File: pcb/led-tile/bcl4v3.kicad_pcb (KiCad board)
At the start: 2 copper layers, 38 x 38 mm, 36 parts, among them J1 Conn_01x04, J10 Conn_01x04, J2 Conn_01x04, J3 Conn_01x04, J4 Conn_01x04, J5 Conn_01x04, J6 Conn_01x04, J7 Conn_01x04, J8 Conn_01x04, J9 10118194-0001LF, Q1 IRLML6402, U1 STM32F072CBTx, U2 74HC595D_118, U3 TBD62783A, U4 TLC5916ID, U5 MCP1703A-3302_SOT23, Y1 ABS07-120-32.768KHZ-Z

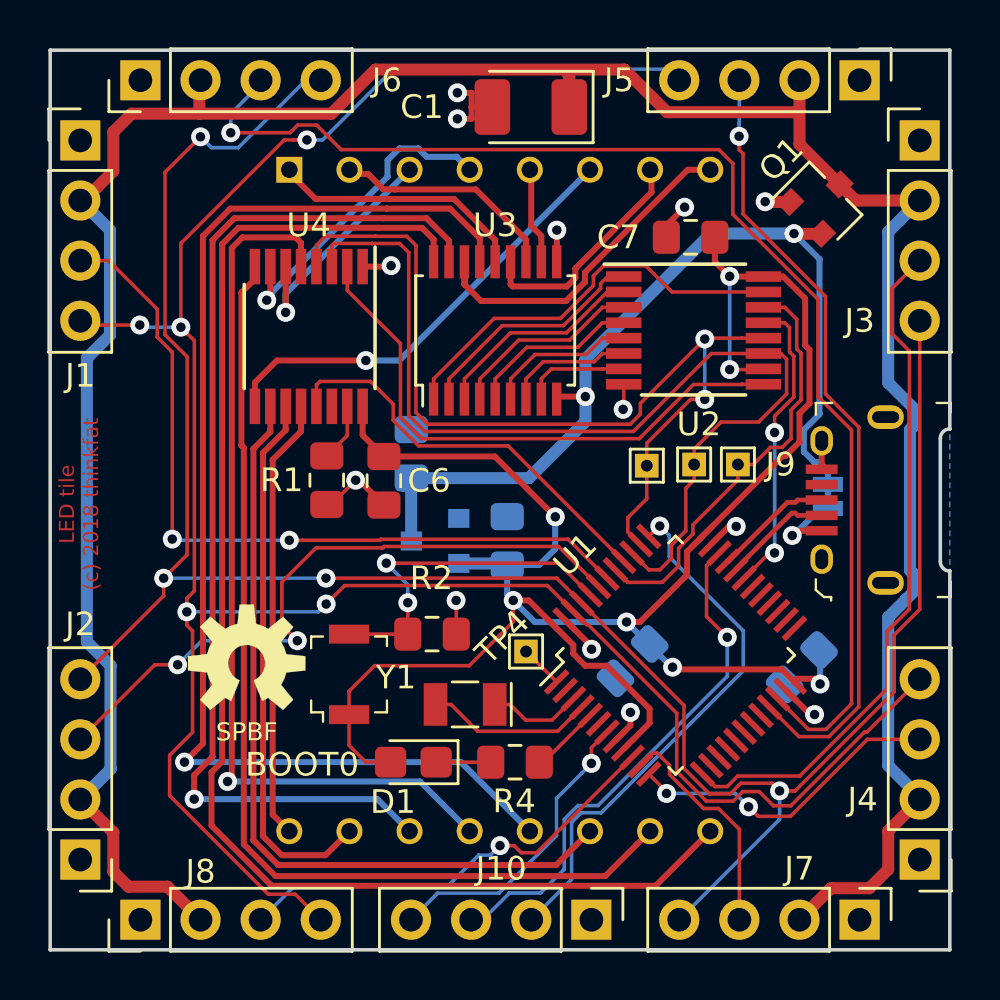
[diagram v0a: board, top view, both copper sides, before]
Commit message: pcb: put USB_VBUS to pin header
Replace one pin header with a 5-contact version and route USB_VBUS
to this pin. Necessary to power a plug-on battery shield from the main
USB connector.
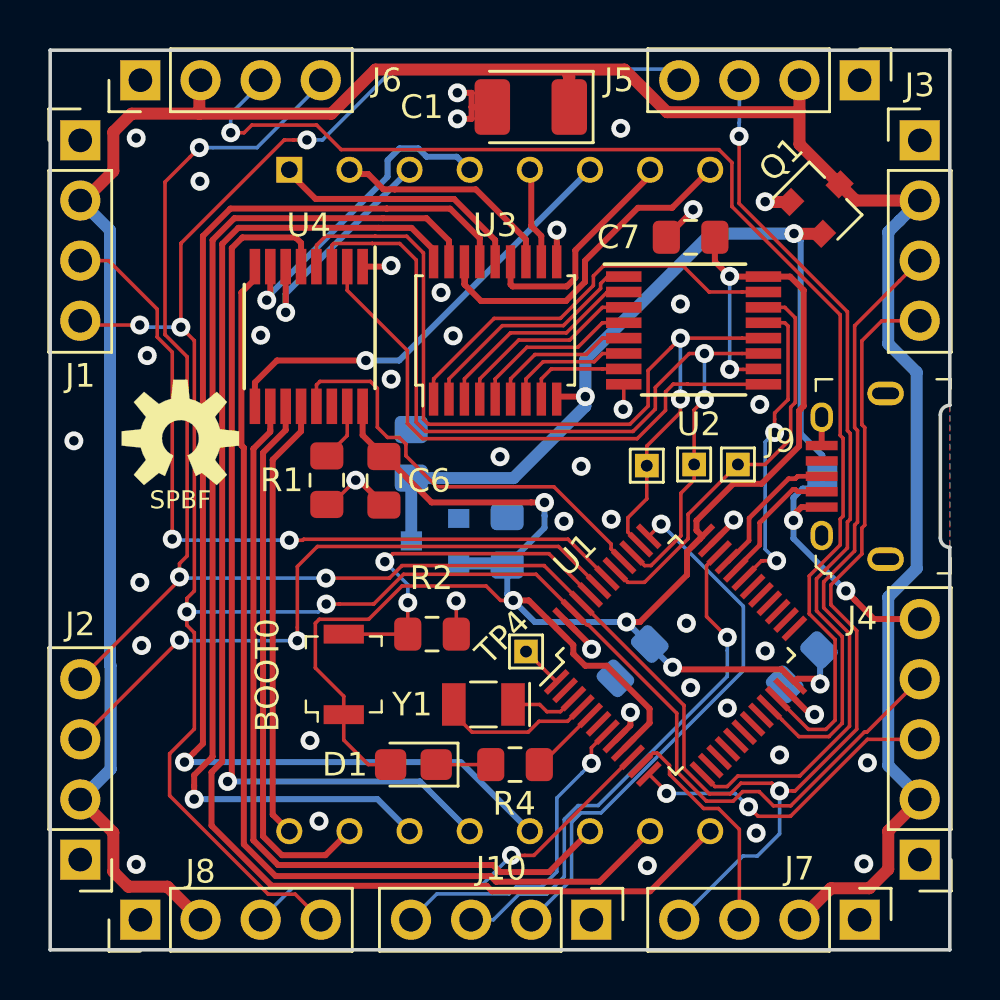
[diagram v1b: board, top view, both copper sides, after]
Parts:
- J4: value Conn_01x04 -> Conn_01x05; footprint Connector_PinHeader_2.54mm:PinHeader_1x04_P2.54mm_Vertical -> Connector_PinHeader_2.54mm:PinHeader_1x05_P2.54mm_Vertical
- moved LOGO1 9.90 mm to (119.5, 80.4)
- moved J9 1.00 mm to (146.6, 82.0)
- moved JP1 0.87 mm to (146.6, 82.0)
- moved Y1 0.77 mm to (132.3, 91.6)
- moved BOOT0 0.22 mm to (126.4, 90.4)
- moved D1 0.10 mm to (129.3, 94.2)
- moved R4 0.10 mm to (133.6, 94.2)
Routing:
- net /USB_VBUS: track 3.51 -> 11.7 mm, vias 1 -> 2
- net +3V3: track 86.0 -> 89.4 mm
- net /CAT_CLK: track 42.4 -> 39.3 mm, vias 0 -> 2
- net +5V: track 39.0 -> 37.0 mm
- net /SYN_RX: track 94.0 -> 95.5 mm
- net /OSC_IN: track 3.97 -> 2.91 mm
- net /nOE_COL: track 17.5 -> 18.5 mm
- net /USB_D+: track 5.05 -> 6.02 mm
- net /USB_D-: track 4.68 -> 5.65 mm
- net /nRST: track 12.9 -> 13.8 mm
- net VCC: track 117.1 -> 116.3 mm
- net /CAT_DATA: track 18.1 -> 17.5 mm
- net /UART3_RX: track 53.6 -> 54.2 mm
- net /UART3_TX: track 33.4 -> 34.0 mm
- net /UART1_RX: track 28.3 -> 27.8 mm
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- added copper zone on F.Cu, net GND
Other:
- outline, holes or cut-outs redrawn
- board text added: "LED tile ©2019 thinkfat"
- board text removed: "LED tile (c) 2018 thinkfat"

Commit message: pcb: update led-tile to latest version
move OSHW logo into a project specific library as not everyone has the
Sparkfun Libraries installed, decrease current through the SMD LED,
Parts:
- LOGO1: footprint Aesthetics:OSHW-LOGO-M -> project:OSHW-LOGO-M
- R4: value 680R -> 715R
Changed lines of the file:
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@@
     (add_net /ROW_8)
+  )
+  (module project:OSHW-LOGO-M (layer F.Cu)
+    (at 119.5 80.4)
+    (descr "OPEN-SOURCE HARDWARE (OSHW) LOGO - MEDIUM - SILKSCREEN")
+    (tags "OPEN-SOURCE HARDWARE (OSHW) LOGO - MEDIUM - SILKSCREEN")
+    (attr virtual)
+    (fp_text reference LOGO1 (at 0 0) (layer F.SilkS) hide
+      (effects (font (size 1 1) (thickness 0.15)))
+    )
+    (fp_text value OSHW-LOGOM (at 0 0) (layer F.SilkS) hide
+      (effects (font (size 1.524 1.524) (thickness 0.15)))
+    )
+    (fp_poly (pts (xy 0.65532 1.5875) (xy 0.90932 1.45542) (xy 1.5367 1.9685) (xy 1.9685 1.5367)
+      (xy 1.45542 0.90932) (xy 1.5875 0.65532) (xy 1.67386 0.38608) (xy 2.47904 0.30226)
+      (xy 2.47904 -0.30226) (xy 1.67386 -0.38608) (xy 1.5875 -0.65532) (xy 1.45542 -0.90932)
+      (xy 1.9685 -1.5367) (xy 1.5367 -1.9685) (xy 0.90932 -1.45542) (xy 0.65532 -1.5875)
+      (xy 0.38608 -1.67386) (xy 0.30226 -2.47904) (xy -0.30226 -2.47904) (xy -0.38608 -1.67386)
+      (xy -0.65532 -1.5875) (xy -0.90932 -1.45542) (xy -1.5367 -1.9685) (xy -1.9685 -1.5367)
+      (xy -1.45542 -0.90932) (xy -1.5875 -0.65532) (xy -1.67386 -0.38608) (xy -2.47904 -0.30226)
+      (xy -2.47904 0.30226) (xy -1.67386 0.38608) (xy -1.5875 0.65532) (xy -1.45542 0.90932)
+      (xy -1.9685 1.5367) (xy -1.5367 1.9685) (xy -0.90932 1.45542) (xy -0.65532 1.5875)
+      (xy -0.29718 0.72136) (xy -0.4318 0.6477) (xy -0.55118 0.55118) (xy -0.6477 0.4318)
+      (xy -0.72136 0.29718) (xy -0.76454 0.1524) (xy -0.77978 0) (xy -0.76454 -0.15748)
+      (xy -0.71374 -0.31242) (xy -0.635 -0.44958) (xy -0.53086 -0.5715) (xy -0.40132 -0.66802)
+      (xy -0.25654 -0.7366) (xy -0.1016 -0.77216) (xy 0.05588 -0.77724) (xy 0.2159 -0.7493)
+      (xy 0.36322 -0.68834) (xy 0.49784 -0.59944) (xy 0.6096 -0.48514) (xy 0.69596 -0.35052)
+      (xy 0.75438 -0.20066) (xy 0.77978 -0.04318) (xy 0.77216 0.1143) (xy 0.73152 0.26924)
+      (xy 0.6604 0.41402) (xy 0.56134 0.54102) (xy 0.43942 0.64516) (xy 0.29718 0.72136)) (layer F.SilkS) (width 0.01))
   )
   (module Connector_PinHeader_2.54mm:PinHeader_1x04_P2.54mm_Vertical (layer F.Cu)
@@
       (effects (font (size 1 1) (thickness 0.15)))
     )
-    (fp_text value 680R (at 0 1.65) (layer F.Fab)
+    (fp_text value 715R (at 0 1.65) (layer F.Fab)
       (effects (font (size 1 1) (thickness 0.15)))
     )
@@
     (pad 1 thru_hole rect (at 0 0) (size 1 1) (drill 0.5) (layers *.Cu *.Mask)
       (net 12 /CAT_STROBE))
-  )
-  (module Aesthetics:OSHW-LOGO-M (layer F.Cu)
-    (at 119.5 80.4)
-    (descr "OPEN-SOURCE HARDWARE (OSHW) LOGO - MEDIUM - SILKSCREEN")
-    (tags "OPEN-SOURCE HARDWARE (OSHW) LOGO - MEDIUM - SILKSCREEN")
-    (attr virtual)
-    (fp_text reference LOGO1 (at 0 0) (layer F.SilkS) hide
-      (effects (font (size 1 1) (thickness 0.15)))
-    )
-    (fp_text value OSHW-LOGOM (at 0 0) (layer F.SilkS) hide
-      (effects (font (size 1.524 1.524) (thickness 0.15)))
-    )
-    (fp_poly (pts (xy 0.65532 1.5875) (xy 0.90932 1.45542) (xy 1.5367 1.9685) (xy 1.9685 1.5367)
-      (xy 1.45542 0.90932) (xy 1.5875 0.65532) (xy 1.67386 0.38608) (xy 2.47904 0.30226)
-      (xy 2.47904 -0.30226) (xy 1.67386 -0.38608) (xy 1.5875 -0.65532) (xy 1.45542 -0.90932)
-      (xy 1.9685 -1.5367) (xy 1.5367 -1.9685) (xy 0.90932 -1.45542) (xy 0.65532 -1.5875)
-      (xy 0.38608 -1.67386) (xy 0.30226 -2.47904) (xy -0.30226 -2.47904) (xy -0.38608 -1.67386)
-      (xy -0.65532 -1.5875) (xy -0.90932 -1.45542) (xy -1.5367 -1.9685) (xy -1.9685 -1.5367)
-      (xy -1.45542 -0.90932) (xy -1.5875 -0.65532) (xy -1.67386 -0.38608) (xy -2.47904 -0.30226)
-      (xy -2.47904 0.30226) (xy -1.67386 0.38608) (xy -1.5875 0.65532) (xy -1.45542 0.90932)
-      (xy -1.9685 1.5367) (xy -1.5367 1.9685) (xy -0.90932 1.45542) (xy -0.65532 1.5875)
-      (xy -0.29718 0.72136) (xy -0.4318 0.6477) (xy -0.55118 0.55118) (xy -0.6477 0.4318)
-      (xy -0.72136 0.29718) (xy -0.76454 0.1524) (xy -0.77978 0) (xy -0.76454 -0.15748)
-      (xy -0.71374 -0.31242) (xy -0.635 -0.44958) (xy -0.53086 -0.5715) (xy -0.40132 -0.66802)
-      (xy -0.25654 -0.7366) (xy -0.1016 -0.77216) (xy 0.05588 -0.77724) (xy 0.2159 -0.7493)
-      (xy 0.36322 -0.68834) (xy 0.49784 -0.59944) (xy 0.6096 -0.48514) (xy 0.69596 -0.35052)
-      (xy 0.75438 -0.20066) (xy 0.77978 -0.04318) (xy 0.77216 0.1143) (xy 0.73152 0.26924)
-      (xy 0.6604 0.41402) (xy 0.56134 0.54102) (xy 0.43942 0.64516) (xy 0.29718 0.72136)) (layer F.SilkS) (width 0.01))
   )
   (module digikey-footprints:USB_Micro_B_Female_10118194-0001LF (layer F.Cu)
@@
   (via (at 124.9744 93.1608) (size 0.8) (drill 0.4) (layers F.Cu B.Cu) (net 8))
   (via (at 133.000798 81.172) (size 0.8) (drill 0.4) (layers F.Cu B.Cu) (net 8))
+  (via (at 148.3678 98.3678) (size 0.8) (drill 0.4) (layers F.Cu B.Cu) (net 8))
   (segment (start 143.603 78.113) (end 144.128 78.113) (width 0.1524) (layer F.Cu) (net 9))
   (segment (start 140.930532 78.113) (end 143.603 78.113) (width 0.1524) (layer F.Cu) (net 9))
@@
   (segment (start 122.647 79.042) (end 122.647 78.038) (width 0.254) (layer F.Cu) (net 17) (status 10))
   (segment (start 122.647 78.038) (end 123.577 77.108) (width 0.254) (layer F.Cu) (net 17))
-  (via (at 148.3678 98.3678) (size 0.8) (drill 0.4) (layers F.Cu B.Cu) (net 8))
   (segment (start 123.297 80.046) (end 123.297 79.042) (width 0.254) (layer F.Cu) (net 18))
   (segment (start 135.072998 98.717002) (end 133.004886 98.717002) (width 0.254) (layer F.Cu) (net 18))

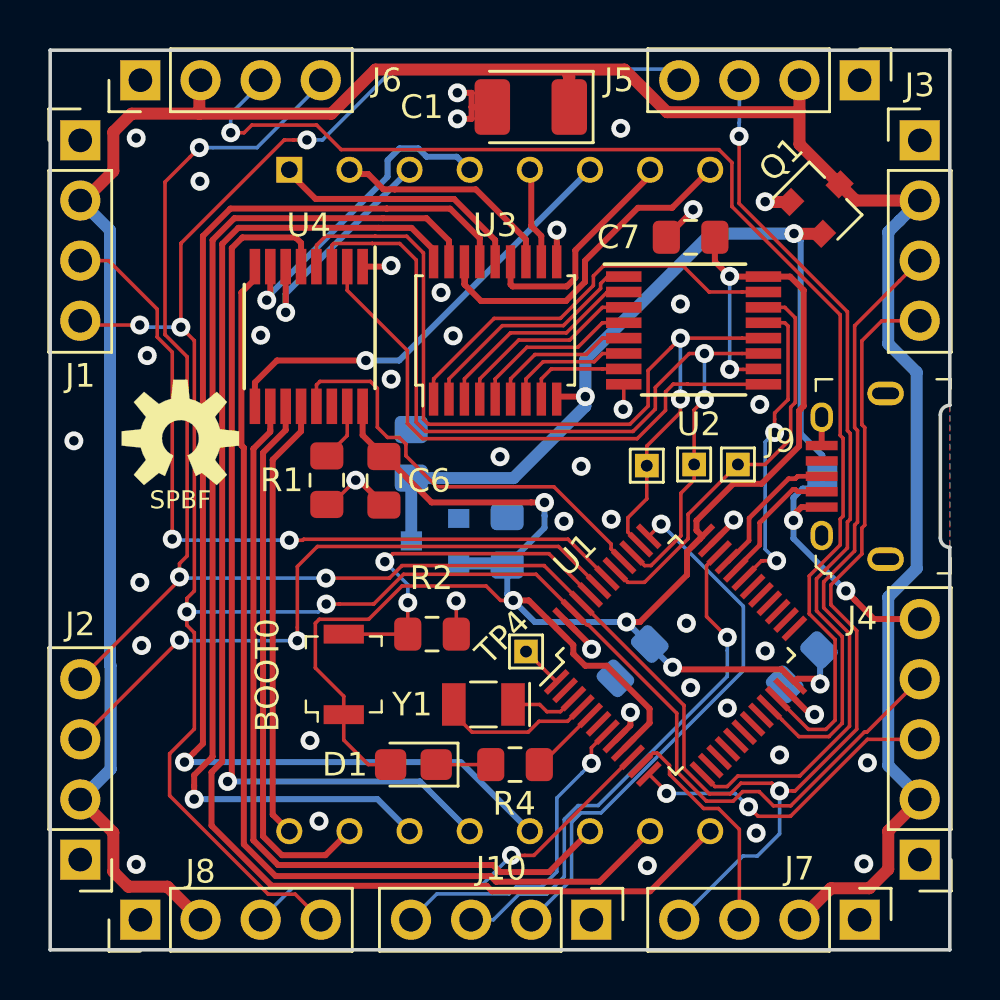
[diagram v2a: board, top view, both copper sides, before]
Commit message: pcb: use IS31FL3730 as matrix driver
reduce component count
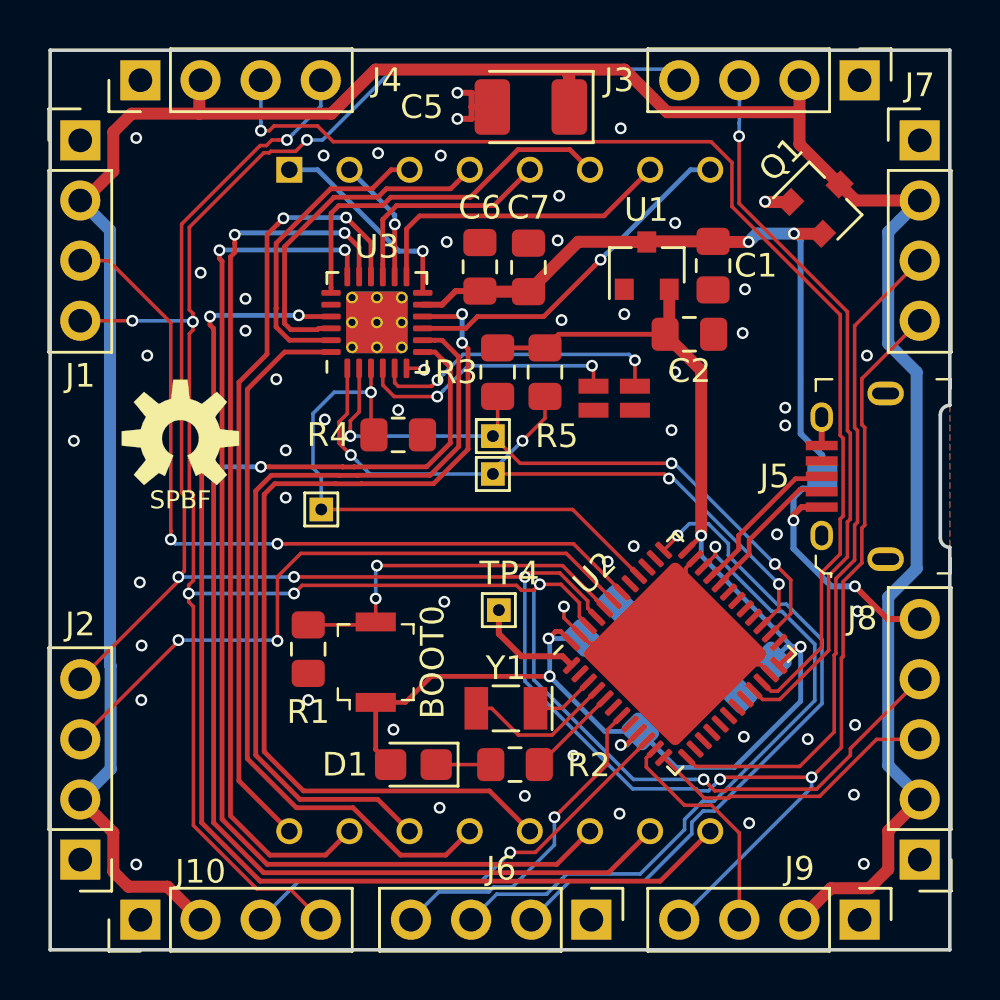
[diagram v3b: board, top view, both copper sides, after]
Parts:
- removed the R1 at (125.7, 82.2)
- removed the U1 at (140.4, 89.6)
- removed U4: TLC5916ID, Package_SO:TSSOP-16_4.4x5mm_P0.65mm
- added C8: 100n, Capacitor_SMD:C_0805_2012Metric_Pad1.15x1.40mm_HandSolder, B.Cu at (137.2, 88.1)
- added JP2: Jumper_2_Open, project:SMT-JUMPER_2_NC_TRACE_NO-SILK, F.Cu at (136.9, 78.7)
- added JP3: Jumper_2_Open, project:SMT-JUMPER_2_NC_TRACE_NO-SILK, F.Cu at (138.7, 78.7)
- added R3: 4k7, Resistor_SMD:R_0805_2012Metric_Pad1.15x1.40mm_HandSolder, F.Cu at (132.9, 77.6)
- added R4: 100k, Resistor_SMD:R_0805_2012Metric_Pad1.15x1.40mm_HandSolder, F.Cu at (128.7, 80.2)
- added R5: 4k7, Resistor_SMD:R_0805_2012Metric_Pad1.15x1.40mm_HandSolder, F.Cu at (134.9, 77.6)
- C1: renamed from C3; moved to F.Cu
- C2: renamed from C4; moved to F.Cu
- C6: value 100n -> 1µF
- U1: renamed from U5; moved to F.Cu
- U2: value 74HC595D_118 -> STM32F072CBUx; footprint Package_SO:TSSOP-16_4.4x5mm_P0.65mm -> Package_DFN_QFN:QFN-48-1EP_7x7mm_P0.5mm_EP5.6x5.6mm
- U3: value TBD62783A -> IS31FL3730-QFSL2; footprint Package_SO:SSOP-18_4.4x6.5mm_P0.65mm -> project:QFN-24-1EP_4x4mm_P0.5mm_EP2.6x2.6mm_ThermalVias
- moved TP3 17.7 mm to (125.5, 83.4)
- moved C1 15.0 mm to (142.0, 73.1), turned to 270 degrees
- moved U1 14.7 mm to (139.2, 73.1), turned to 90 degrees
- moved U2 13.7 mm to (140.4, 89.5), turned to 45 degrees
- moved C2 11.6 mm to (141.0, 76.0), turned to 0 degrees
- moved C6 9.91 mm to (132.2, 73.2), turned to 90 degrees
- moved TP1 8.58 mm to (132.7, 80.3)
- moved C7 6.97 mm to (134.2, 73.2), turned to 90 degrees
- moved TP2 6.51 mm to (132.7, 81.9)
- moved R1 5.27 mm to (124.9, 89.3), turned to 270 degrees
- moved U3 5.01 mm to (127.8, 75.5)
- moved C3 2.48 mm to (139.7, 92.0), turned to 45 degrees
- moved TP4 2.09 mm to (132.9, 87.7)
- moved C4 2.00 mm to (143.8, 90.5)
- moved BOOT0 1.45 mm to (127.8, 89.8)
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- renumbered C5 to C3, C8 to C4, C1 to C5, J8 to J10, J5 to J3, J6 to J4, J9 to J5, J10 to J6, J3 to J7, J4 to J8, J7 to J9, R2 to R1, R4 to R2
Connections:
- C6 pad 1: +3V3 -> +5V
- C7 pad 1: +3V3 -> +5V
- TP1 pad 1: /CAT_CLK -> /MCU_SCL
- TP2 pad 1: /CAT_STROBE -> /MCU_SDA
- TP3 pad 1: /CAT_DATA -> /MCU_SDB
- U2 pad 1: Net-(U2-Pad1) -> /VBAT
- U2 pad 10: +3V3 -> /UART4_TX
- U2 pad 11: /CAT_CLK -> /UART4_RX
- U2 pad 12: /CAT_STROBE -> /UART2_TX
- U2 pad 13: /nOE_ROW -> /UART2_RX
- U2 pad 14: /CAT_DATA -> Net-(U2-Pad14)
- U2 pad 16: +3V3 -> Net-(U2-Pad16)
- U2 pad 3: Net-(U2-Pad3) -> /OSC_IN
- U2 pad 4: Net-(U2-Pad4) -> /OSC_OUT
- U2 pad 5: Net-(U2-Pad5) -> /LED
- U2 pad 7: Net-(U2-Pad7) -> /nRST
- U2 pad 8: GND -> Net-(U2-Pad8)
- U2 pad 9: Net-(U2-Pad9) -> +3V3
- U3 pad 1: Net-(U2-Pad15) -> /MCU_SDA
- U3 pad 10: GND -> /ROW_4
- U3 pad 11: /ROW_8 -> +5V
- U3 pad 12: /ROW_7 -> /ROW_5
- U3 pad 14: /ROW_5 -> /ROW_7
- U3 pad 15: /ROW_4 -> /ROW_8
- U3 pad 16: /ROW_3 -> /COL_8
- U3 pad 17: /ROW_2 -> /COL_7
- U3 pad 18: /ROW_1 -> /COL_6
- U3 pad 2: Net-(U2-Pad1) -> /MCU_SCL
- U3 pad 3: Net-(U2-Pad2) -> /MCU_SDB
- U3 pad 4: Net-(U2-Pad3) -> Net-(JP2-Pad2)
- U3 pad 5: Net-(U2-Pad4) -> Net-(JP3-Pad2)
- U3 pad 6: Net-(U2-Pad5) -> GND
- U3 pad 7: Net-(U2-Pad6) -> /ROW_1
- U3 pad 8: Net-(U2-Pad7) -> /ROW_2
- U3 pad 9: +5V -> /ROW_3
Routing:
- net /CAT_STROBE: track 39.6 -> 0.00 mm, vias 2 -> 0
- net /CAT_CLK: track 39.3 -> 0.00 mm, vias 2 -> 0
- net /MCU_SDA: track 0.00 -> 30.6 mm, vias 0 -> 4
- net /MCU_SCL: track 0.00 -> 28.5 mm, vias 0 -> 3
- net +3V3: track 89.4 -> 61.9 mm, vias 7 -> 5
- net Net-(U2-Pad9): track 24.4 -> 0.00 mm
- net /MCU_SDB: track 0.00 -> 24.0 mm, vias 0 -> 1
- net /nOE_COL: track 18.5 -> 0.00 mm
- net /CAT_DATA: track 17.5 -> 0.00 mm
- net Net-(U2-Pad15): track 17.3 -> 0.00 mm
- net /COL_7: track 23.0 -> 37.5 mm, vias 0 -> 2
- net /COL_8: track 18.7 -> 33.1 mm, vias 0 -> 2
- net /COL_6: track 34.1 -> 47.5 mm, vias 0 -> 2
- net /nOE_ROW: track 13.3 -> 0.00 mm, vias 2 -> 0
- net Net-(JP3-Pad2): track 0.00 -> 12.6 mm, vias 0 -> 2
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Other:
- net class Default: via_dia 0.8 -> 0.5; via_drill 0.4 -> 0.3
- net class VCC: via_dia 0.8 -> 0.5; via_drill 0.4 -> 0.3
- net class VCC_LOW: trace_width 0.254 -> 0.2032; via_dia 0.8 -> 0.5; via_drill 0.4 -> 0.3
- rule via_min_drill: 0.4 -> 0.3
